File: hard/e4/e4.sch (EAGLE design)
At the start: 16 parts

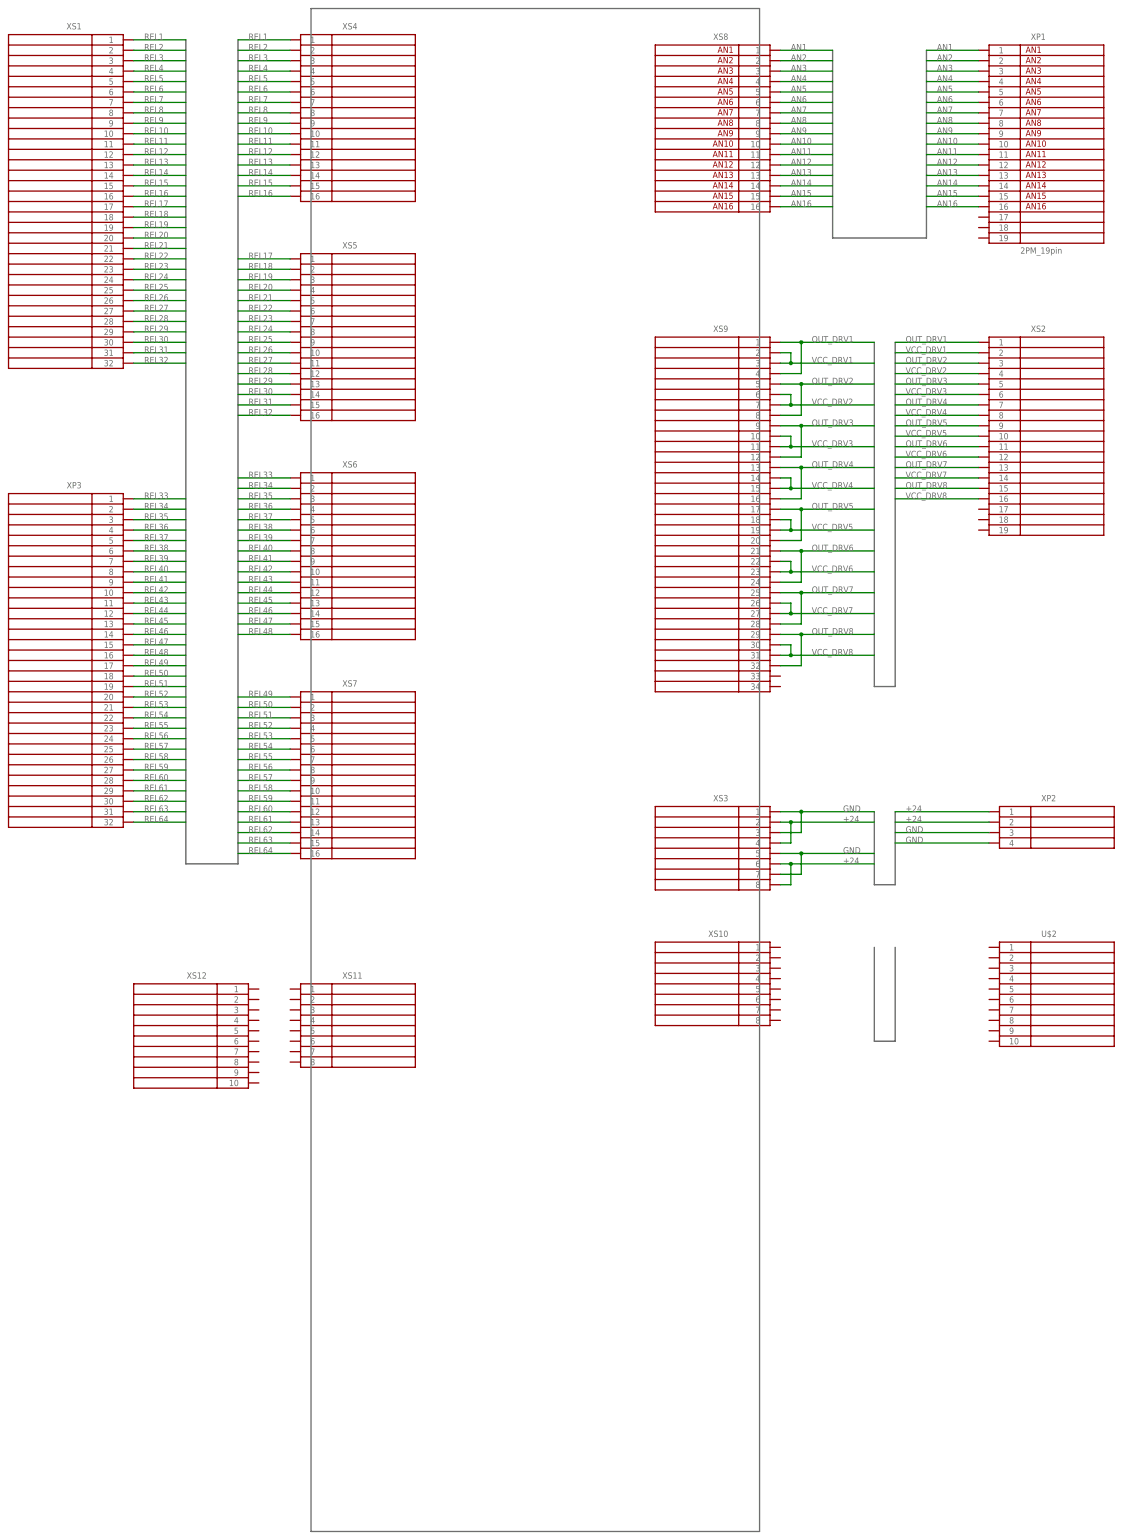
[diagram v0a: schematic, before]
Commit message: moved e4 to separate dir
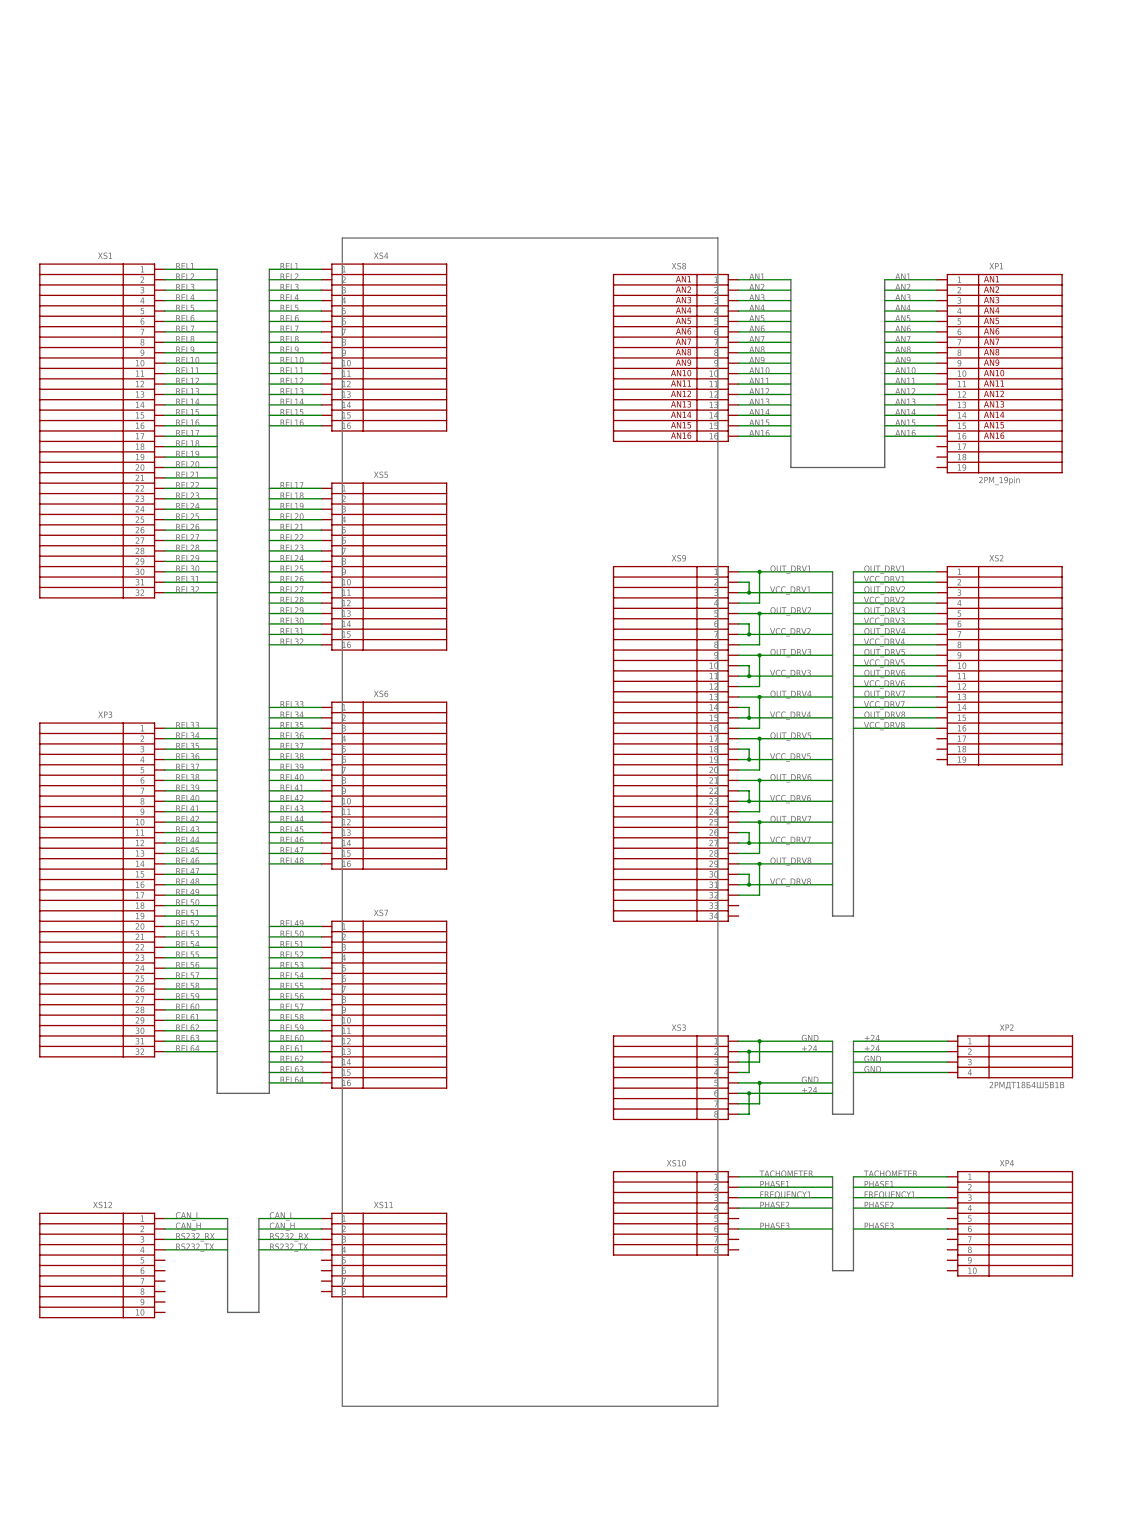
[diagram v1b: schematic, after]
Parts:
- removed U$2: (no value), connector:GENERIC_10_XP
- added XP4: (no value), connector:GENERIC_10_XP
- XP2: value (none) -> 2РМДТ18Б4Ш5В1В
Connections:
- new net CAN_H: XS11.2, XS12.2
- new net CAN_L: XS11.1, XS12.1
- new net FREQUENCY1: XP4.3, XS10.3
- new net PHASE1: XP4.2, XS10.2
- new net PHASE2: XP4.4, XS10.4
- new net PHASE3: XP4.6, XS10.6
- new net RS232_RX: XS11.3, XS12.3
- new net RS232_TX: XS11.4, XS12.4
- new net TACHOMETER: XP4.1, XS10.1
- net AN1: now also XP1.1
- net AN10: now also XP1.10
- net AN11: now also XP1.11
- net AN12: now also XP1.12
- net AN13: now also XP1.13
- net AN14: now also XP1.14
- net AN15: now also XP1.15
- net AN16: now also XP1.16
- net AN2: now also XP1.2
- net AN3: now also XP1.3
- net AN4: now also XP1.4
- net AN5: now also XP1.5
- net AN6: now also XP1.6
- net AN7: now also XP1.7
- net AN8: now also XP1.8
- net AN9: now also XP1.9
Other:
- moved on the sheet: XP1, XP2, XP3, XS1, XS10, XS11, XS12, XS2, XS3, XS4, XS5, XS6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

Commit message: e4 improvements
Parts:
- XP1: value 2PM_19pin -> 2РМДТ27Б19Г5В1В
- XP3: value (none) -> 2РМДТ33Б32Г5В1В
- XP4: value (none) -> 2РМТ22Б10Г1В1В
- XS1: value (none) -> 2РМДТ33Б32Ш5В1В
- XS10, XS11, XS3: value (none) -> 90142-0008; PARTNO (none) -> 90142-0008
- XS12: value (none) -> 2РМТ22Б10Ш1В1В
- XS2: value (none) -> 2РМДТ27Б19Ш5В1В
- XS4, XS5, XS6, XS7, XS8: value (none) -> 90142-0016; PARTNO (none) -> 90142-0016
- XS9: value (none) -> 90142-0034; PARTNO (none) -> 90142-0034
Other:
- note added: "Для обжима использовать контакты типа 00000 "Molex""
- note added: "Плата КСАУ.666666.000"
- note added: "Цепи выполнить проводом МГТФ 0.35"
- moved on the sheet: XP1, XP2, XP4, XS10, XS11, XS12, XS2, XS3, XS8, XS9

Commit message: nop
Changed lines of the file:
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@@
 <setting verticaltext="up"/>
 </settings>
-<grid distance="0.025" unitdist="inch" unit="inch" style="lines" multiple="1" display="yes" altdistance="0.01" altunitdist="inch" altunit="inch"/>
+<grid distance="0.1" unitdist="inch" unit="inch" style="lines" multiple="1" display="yes" altdistance="0.01" altunitdist="inch" altunit="inch"/>
 <layers>
 <layer number="1" name="Top" color="4" fill="1" visible="no" active="no"/>
@@
 <text x="17.78" y="7.62" size="1.524" layer="94">Для обжима использовать контакты типа 00000 "Molex"</text>
 <text x="132.08" y="370.84" size="1.524" layer="94">Плата КСАУ.666666.000</text>
-<wire x1="101.6" y1="88.9" x2="101.6" y2="111.76" width="0.1524" layer="94"/>
-<wire x1="193.04" y1="88.9" x2="193.04" y2="134.62" width="0.1524" layer="94"/>
-<wire x1="193.04" y1="88.9" x2="101.6" y2="88.9" width="0.1524" layer="94"/>
-<wire x1="101.6" y1="375.92" x2="101.6" y2="345.44" width="0.1524" layer="94"/>
-<wire x1="193.04" y1="375.92" x2="193.04" y2="345.44" width="0.1524" layer="94"/>
-<wire x1="101.6" y1="375.92" x2="193.04" y2="375.92" width="0.1524" layer="94"/>
-<wire x1="101.6" y1="302.26" x2="101.6" y2="292.1" width="0.1524" layer="94"/>
-<wire x1="101.6" y1="248.92" x2="101.6" y2="238.76" width="0.1524" layer="94"/>
-<wire x1="101.6" y1="195.58" x2="101.6" y2="185.42" width="0.1524" layer="94"/>
-<wire x1="101.6" y1="142.24" x2="101.6" y2="134.62" width="0.1524" layer="94"/>
-<wire x1="193.04" y1="157.48" x2="193.04" y2="167.64" width="0.1524" layer="94"/>
-<wire x1="193.04" y1="190.5" x2="193.04" y2="198.12" width="0.1524" layer="94"/>
-<wire x1="193.04" y1="287.02" x2="193.04" y2="302.26" width="0.1524" layer="94"/>
+<wire x1="104.14" y1="88.9" x2="104.14" y2="111.76" width="0.1524" layer="94"/>
+<wire x1="190.5" y1="88.9" x2="190.5" y2="134.62" width="0.1524" layer="94"/>
+<wire x1="190.5" y1="88.9" x2="104.14" y2="88.9" width="0.1524" layer="94"/>
+<wire x1="104.14" y1="375.92" x2="104.14" y2="345.44" width="0.1524" layer="94"/>
+<wire x1="190.5" y1="375.92" x2="190.5" y2="345.44" width="0.1524" layer="94"/>
+<wire x1="104.14" y1="375.92" x2="190.5" y2="375.92" width="0.1524" layer="94"/>
+<wire x1="104.14" y1="302.26" x2="104.14" y2="292.1" width="0.1524" layer="94"/>
+<wire x1="104.14" y1="248.92" x2="104.14" y2="238.76" width="0.1524" layer="94"/>
+<wire x1="104.14" y1="195.58" x2="104.14" y2="185.42" width="0.1524" layer="94"/>
+<wire x1="104.14" y1="142.24" x2="104.14" y2="134.62" width="0.1524" layer="94"/>
+<wire x1="190.5" y1="157.48" x2="190.5" y2="167.64" width="0.1524" layer="94"/>
+<wire x1="190.5" y1="190.5" x2="190.5" y2="198.12" width="0.1524" layer="94"/>
+<wire x1="190.5" y1="287.02" x2="190.5" y2="302.26" width="0.1524" layer="94"/>
 </plain>
 <instances>

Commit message: e4 improvements
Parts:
- XP1: value 2РМДТ27Б19Г5В1В -> 2РМДТ33Б32Г5В1В; device connector:GENERIC_19_XP -> connector:GENERIC_32_XP
- XP2: value 2РМДТ18Б4Ш5В1В -> 2РМДТ27Б19Г5В1В; device connector:GENERIC_04_XP -> connector:GENERIC_19_XP
- XP3: value 2РМДТ33Б32Г5В1В -> 2РМДТ18Б4Ш5В1В; device connector:GENERIC_32_XP -> connector:GENERIC_04_XP
- XS12: value 2РМТ22Б10Ш1В1В -> 2РМДТ27Б19Ш5В1В; device connector:GENERIC_10_XS -> connector:GENERIC_19_XS
- XS2: value 2РМДТ27Б19Ш5В1В -> 2РМТ22Б10Ш1В1В; device connector:GENERIC_19_XS -> connector:GENERIC_10_XS
- XS3: value 90142-0008 -> 90142-0016; device connector:GENERIC_08_XS -> connector:GENERIC_16_XS; PARTNO 90142-0008 -> 90142-0016
- XS7: value 90142-0016 -> 90142-0008; device connector:GENERIC_16_XS -> connector:GENERIC_08_XS; PARTNO 90142-0016 -> 90142-0008
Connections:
- net +24: now also XP3.1, XP3.2, XS10.2, XS10.4, XS10.6, XS10.8; no longer XP2.1, XP2.2, XS3.2, XS3.4, XS3.6, XS3.8
- net AN1: now also XP2.1; no longer XP1.1
- net AN10: now also XP2.10; no longer XP1.10
- net AN11: now also XP2.11; no longer XP1.11
- net AN12: now also XP2.12; no longer XP1.12
- net AN13: now also XP2.13; no longer XP1.13
- net AN14: now also XP2.14; no longer XP1.14
- net AN15: now also XP2.15; no longer XP1.15
- net AN16: now also XP2.16; no longer XP1.16
- net AN2: now also XP2.2; no longer XP1.2
- net AN3: now also XP2.3; no longer XP1.3
- net AN4: now also XP2.4; no longer XP1.4
- net AN5: now also XP2.5; no longer XP1.5
- net AN6: now also XP2.6; no longer XP1.6
- net AN7: now also XP2.7; no longer XP1.7
- net AN8: now also XP2.8; no longer XP1.8
- net AN9: now also XP2.9; no longer XP1.9
- net CAN_H: now also XS2.2, XS7.2; no longer XS11.2, XS12.2
- net CAN_L: now also XS2.1, XS7.1; no longer XS11.1, XS12.1
- net FREQUENCY1: now also XS11.3; no longer XS10.3
- net GND: now also XP3.3, XP3.4, XS10.1, XS10.3, XS10.5, XS10.7; no longer XP2.3, XP2.4, XS3.1, XS3.3, XS3.5, XS3.7
- net OUT_DRV1: now also XS12.1; no longer XS2.1
- net OUT_DRV2: now also XS12.3; no longer XS2.3
- net OUT_DRV3: now also XS12.5; no longer XS2.5
- net OUT_DRV4: now also XS12.7; no longer XS2.7
- net OUT_DRV5: now also XS12.9; no longer XS2.9
- net OUT_DRV6: now also XS12.11; no longer XS2.11
- net OUT_DRV7: now also XS12.13; no longer XS2.13
- net OUT_DRV8: now also XS12.15; no longer XS2.15
- net PHASE1: now also XS11.2; no longer XS10.2
- net PHASE2: now also XS11.4; no longer XS10.4
- net PHASE3: now also XS11.6; no longer XS10.6
- net REL1: now also XS3.1; no longer XS4.1
- net REL10: now also XS3.10; no longer XS4.10
- net REL11: now also XS3.11; no longer XS4.11
- net REL12: now also XS3.12; no longer XS4.12
- net REL13: now also XS3.13; no longer XS4.13
- net REL14: now also XS3.14; no longer XS4.14
- net REL15: now also XS3.15; no longer XS4.15
- net REL16: now also XS3.16; no longer XS4.16
- net REL17: now also XS4.1; no longer XS5.1
- net REL18: now also XS4.2; no longer XS5.2
- net REL19: now also XS4.3; no longer XS5.3
- net REL2: now also XS3.2; no longer XS4.2
- net REL20: now also XS4.4; no longer XS5.4
- net REL21: now also XS4.5; no longer XS5.5
- net REL22: now also XS4.6; no longer XS5.6
- net REL23: now also XS4.7; no longer XS5.7
- net REL24: now also XS4.8; no longer XS5.8
- net REL25: now also XS4.9; no longer XS5.9
- net REL26: now also XS4.10; no longer XS5.10
- net REL27: now also XS4.11; no longer XS5.11
- net REL28: now also XS4.12; no longer XS5.12
- net REL29: now also XS4.13; no longer XS5.13
- net REL3: now also XS3.3; no longer XS4.3
- net REL30: now also XS4.14; no longer XS5.14
- net REL31: now also XS4.15; no longer XS5.15
- net REL32: now also XS4.16; no longer XS5.16
- net REL33: now also XP1.1, XS5.1; no longer XP3.1, XS6.1
- net REL34: now also XP1.2, XS5.2; no longer XP3.2, XS6.2
- net REL35: now also XP1.3, XS5.3; no longer XP3.3, XS6.3
- net REL36: now also XP1.4, XS5.4; no longer XP3.4, XS6.4
- net REL37: now also XP1.5, XS5.5; no longer XP3.5, XS6.5
- net REL38: now also XP1.6, XS5.6; no longer XP3.6, XS6.6
- net REL39: now also XP1.7, XS5.7; no longer XP3.7, XS6.7
- net REL4: now also XS3.4; no longer XS4.4
- net REL40: now also XP1.8, XS5.8; no longer XP3.8, XS6.8
- net REL41: now also XP1.9, XS5.9; no longer XP3.9, XS6.9
- net REL42: now also XP1.10, XS5.10; no longer XP3.10, XS6.10
- net REL43: now also XP1.11, XS5.11; no longer XP3.11, XS6.11
- net REL44: now also XP1.12, XS5.12; no longer XP3.12, XS6.12
- net REL45: now also XP1.13, XS5.13; no longer XP3.13, XS6.13
- net REL46: now also XP1.14, XS5.14; no longer XP3.14, XS6.14
- net REL47: now also XP1.15, XS5.15; no longer XP3.15, XS6.15
- net REL48: now also XP1.16, XS5.16; no longer XP3.16, XS6.16
- net REL49: now also XP1.17, XS6.1; no longer XP3.17, XS7.1
- net REL5: now also XS3.5; no longer XS4.5
- net REL50: now also XP1.18, XS6.2; no longer XP3.18, XS7.2
- net REL51: now also XP1.19, XS6.3; no longer XP3.19, XS7.3
- net REL52: now also XP1.20, XS6.4; no longer XP3.20, XS7.4
- net REL53: now also XP1.21, XS6.5; no longer XP3.21, XS7.5
- net REL54: now also XP1.22, XS6.6; no longer XP3.22, XS7.6
- net REL55: now also XP1.23, XS6.7; no longer XP3.23, XS7.7
- net REL56: now also XP1.24, XS6.8; no longer XP3.24, XS7.8
- net REL57: now also XP1.25, XS6.9; no longer XP3.25, XS7.9
- net REL58: now also XP1.26, XS6.10; no longer XP3.26, XS7.10
- net REL59: now also XP1.27, XS6.11; no longer XP3.27, XS7.11
- net REL6: now also XS3.6; no longer XS4.6
- net REL60: now also XP1.28, XS6.12; no longer XP3.28, XS7.12
- net REL61: now also XP1.29, XS6.13; no longer XP3.29, XS7.13
- net REL62: now also XP1.30, XS6.14; no longer XP3.30, XS7.14
- net REL63: now also XP1.31, XS6.15; no longer XP3.31, XS7.15
- net REL64: now also XP1.32, XS6.16; no longer XP3.32, XS7.16
- net REL7: now also XS3.7; no longer XS4.7
- net REL8: now also XS3.8; no longer XS4.8
- net REL9: now also XS3.9; no longer XS4.9
- net RS232_RX: now also XS2.3, XS7.3; no longer XS11.3, XS12.3
- net RS232_TX: now also XS2.4, XS7.4; no longer XS11.4, XS12.4
- net TACHOMETER: now also XS11.1; no longer XS10.1
- net VCC_DRV1: now also XS12.2; no longer XS2.2
- net VCC_DRV2: now also XS12.4; no longer XS2.4
- net VCC_DRV3: now also XS12.6; no longer XS2.6
- net VCC_DRV4: now also XS12.8; no longer XS2.8
- net VCC_DRV5: now also XS12.10; no longer XS2.10
- net VCC_DRV6: now also XS12.12; no longer XS2.12
- net VCC_DRV7: now also XS12.14; no longer XS2.14
- net VCC_DRV8: now also XS12.16; no longer XS2.16
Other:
- note added: "XP10"
- note added: "XP11"
- note added: "XP12"
- note added: "XP4"
- note added: "XP5"
- note added: "XP6"
- note added: "XP7"
- note added: "XP8"
- note added: "XP9"
- note added: "Для обжима использовать контакты типа 90119-2110 "Molex""
- note added: "Плата КСАУ.123456.000"
- note removed: "Для обжима использовать контакты типа 00000 "Molex""
- note removed: "Плата КСАУ.666666.000"
- moved on the sheet: XS10, XS11, XS4, XS5, XS6
